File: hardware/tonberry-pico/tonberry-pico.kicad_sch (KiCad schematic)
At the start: 30 parts, among them J1 MicroSD_Breakout, J2 SparkFun I2S Audio Breakout M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, J3 RC522_Breakout, J4 Adafruit_bq25185_5V, J5 UART, J6 WS2812, J7 Buttons, J8 Conn_01x01, Q1 2N7000, Q2 2N7000, SW1 SW_Push, SW2 SW_Push, SW3 SW_Push, SW4 SW_Push, SW5 SW_Push, SW6 SW_Push, U1 RaspberryPi_Pico_W

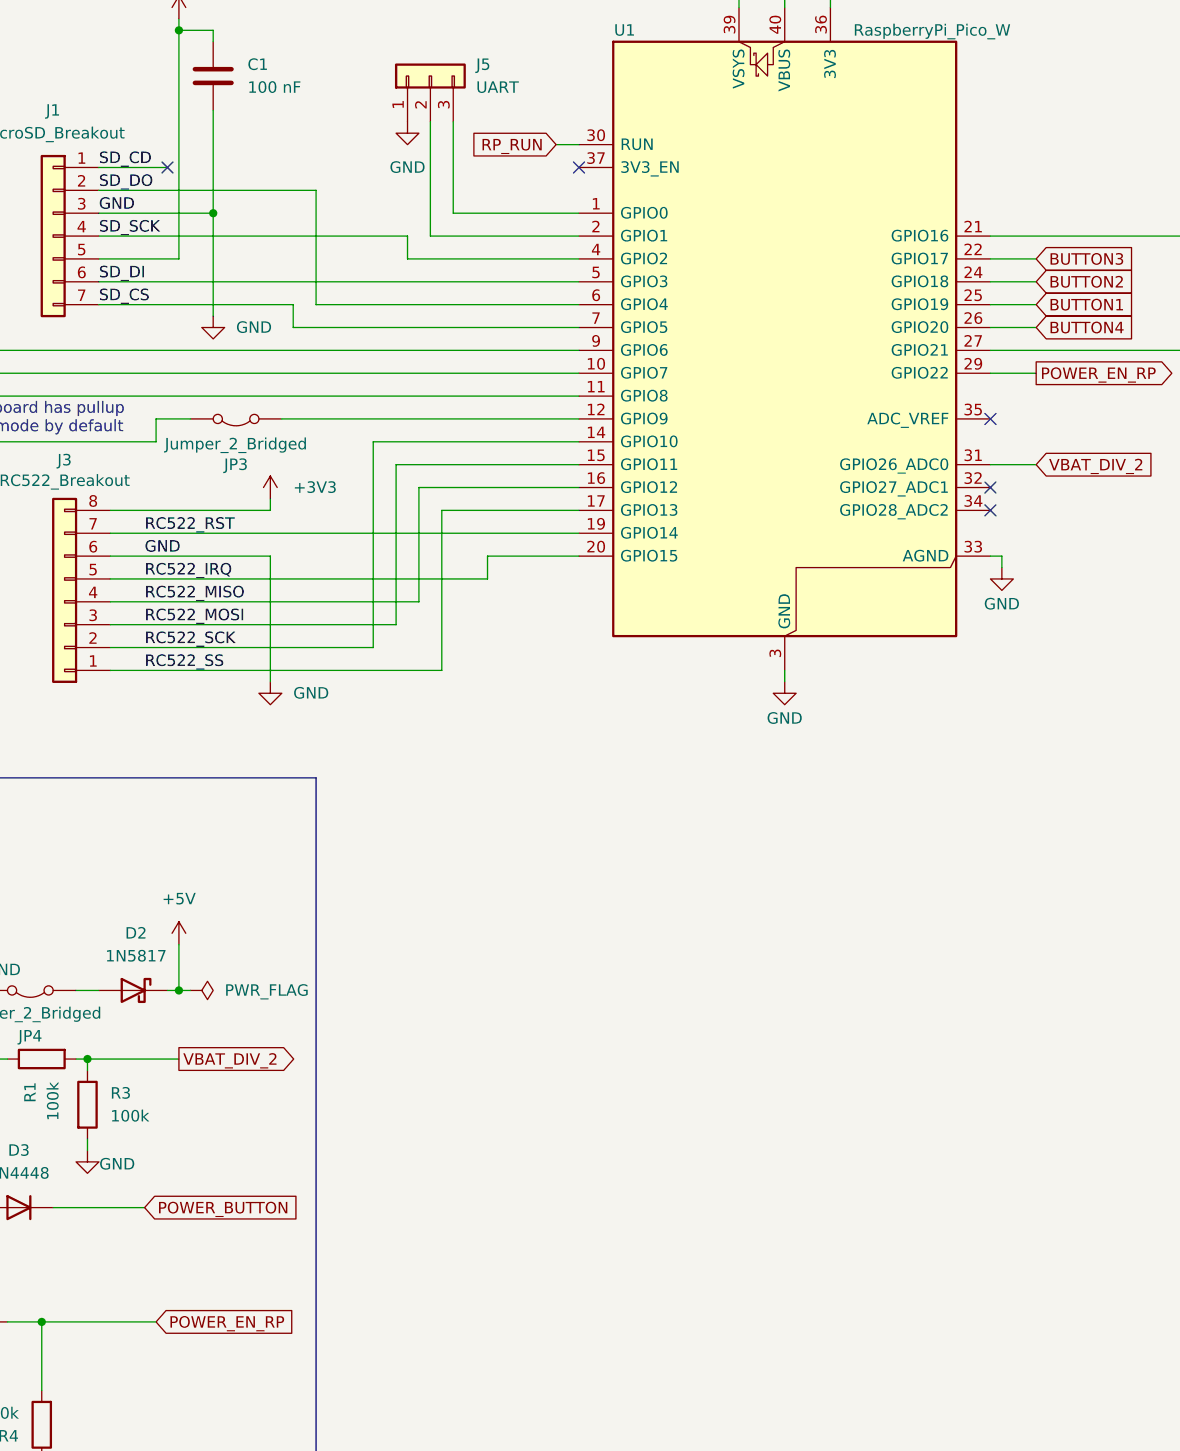
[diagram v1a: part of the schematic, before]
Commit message: this adds the footprint of the microSD card socket (same as sparkfun_microSD_Transflash_Breakout) so that it could be used optionally, since the original sparkfun_microSD_Transflash_Breakout is not available anymore. This part is just about manually solderable, the chips on the other breakout boards maybe less so. Let's order this and see how it fares :)
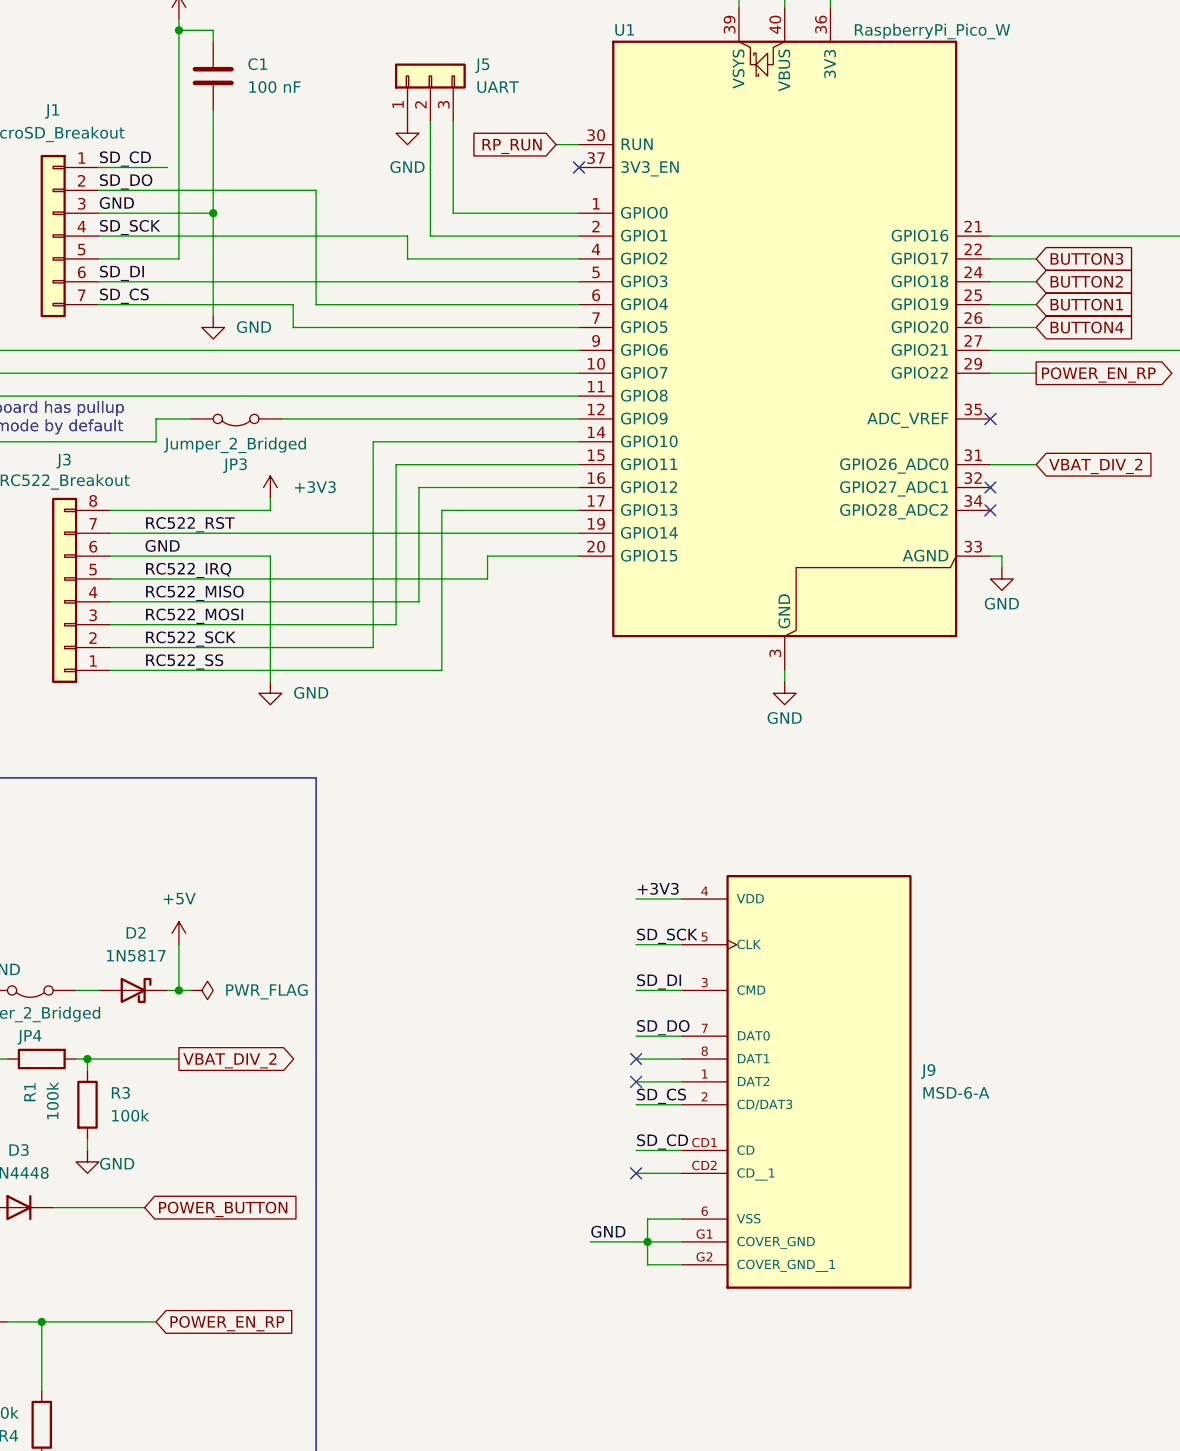
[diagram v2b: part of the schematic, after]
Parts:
- added J9: MSD-6-A, MSD-6-A:CUI_MSD-6-A, symbol MSD-6-A:MSD-6-A
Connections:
- net +3V3: now also J9.4 (VDD)
- net GND: now also J9.6 (VSS), J9.G1 (COVER_GND), J9.G2 (COVER_GND__1)
- net SD_CD: now also J9.CD1 (CD)
- net SD_CS: now also J9.2 (CD/DAT3)
- net SD_DI: now also J9.3 (CMD)
- net SD_DO: now also J9.7 (DAT0)
- net SD_SCK: now also J9.5 (CLK)
- no-connect marks 8 -> 10
